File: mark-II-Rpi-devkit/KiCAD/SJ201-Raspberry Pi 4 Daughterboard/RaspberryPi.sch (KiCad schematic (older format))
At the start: 66 parts, among them J6 Raspberry_Pi_4, J7 USB_B_Micro, P1 LED, P2 LED, P3 LED, P4 LED, SW1 MuteMic, U6 FE1.1s, Y2 12MHz

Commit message: SJ201 - Removed CM108b soundcard, added in I2S to Line out, ATTin402. Moved holes in layout. SJ202 - extened length to plug into USB2.0 port
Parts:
- removed TP0, TP1, TP10, TP11, TP12, TP13, TP14, TP15, TP16, TP17, TP19, TP20, TP21, TP26, TP27, TP4, TP5, TP6, TP7, TP8, TP9: TestPoint, TestPoint:TestPoint_Pad_D1.0mm, symbol Connector:TestPoint
- added J13: USB-PinHeader, Connector_PinSocket_2.54mm:PinSocket_1x04_P2.54mm_Horizontal, symbol Connector_Generic:Conn_01x04
- added Prog1: Prog, TestPoint:TestPoint_Pad_D2.0mm, symbol Connector:TestPoint
- added U14: ATtiny402-SS, Package_SO:SOIC-8_3.9x4.9mm_P1.27mm, symbol MCU_Microchip_ATtiny:ATtiny402-SS
- ACT1, P1, P2, P4: MPN 19-217-R6C-AL1M2VY-3T -> 19-217/GHC-YR1S2/3T; SKU 304090042 -> (none)
- D10, D11, D12, D13, D2, D3, D4, D5, D6, D7, D8, D9: LCSC C114583 -> C527089
- DM3, DP3, TP18, TP2, TP3, USB_Power1: MPN (none) -> DNP
- P3: SKU 304090042 -> (none)
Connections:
- net labels added: ATTinyProg, D+, D-, SCL, SDA, USB_MICRO_D+, USB_MICRO_D-
- net labels removed: USB_SOUNDCARD_D+, USB_SOUNDCARD_D-
- wire segments 138 -> 142
- no-connect marks 8 -> 27
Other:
- moved on the sheet: S1, S2, S3, SW1, TP2, TP3

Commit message: SJ-201 v3, sent to PCB Fab. Removed USB Hub, add in I2S to Line Out
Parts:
- removed USB_Power1: USB Jumper, Jumper:SolderJumper-2_P1.3mm_Open_TrianglePad1.0x1.5mm, symbol Connector_Generic:Conn_01x02
- added R12, R13, R14, R15, R16, R19, R9: 0R, Resistor_SMD:R_0603_1608Metric, symbol Device:R_Small
- added R57: 0R - DNP, Resistor_SMD:R_0603_1608Metric, symbol Device:R_Small
- J13: Tempo (none) -> PPTC041LGBN-RC
- J7: Link (none) -> https://www.newark.com/gct-global-connector-technology/usb3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; MPN U254-051T-4BH83-F1B -> USB3076-30-A; Vendor (none) -> Newark
- R30: Tempo (none) -> ERJ-2GEJ104X
- R31: Tempo (none) -> RC0603FR-072K7L
- S1: value Action -> Button
- S2: value VolUp -> Button
- S3: value VolDown -> Button
- Y2: Tempo (none) -> CX3225GB12000D0HEQZ1
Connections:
- net labels added: USB_CORAL_D+, USB_CORAL_D-
- net labels removed: USB_MICRO_D+, USB_MICRO_D-
- wire segments 142 -> 156
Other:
- moved on the sheet: Prog1

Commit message: Rev4 Update - Add in Coral TPU, TAS5806, remove I2S * MAX9744. Change Attiny to Attin1614
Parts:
- removed ACT1, P1, P2, P3, P4: LED, LED_SMD:LED_0603_1608Metric, symbol Device:LED
- removed J7: USB_B_Micro, user:USB_Micro-B_GCT_USB3076-30-A, symbol Connector:USB_B_Micro
- removed Prog1: Prog, TestPoint:TestPoint_Pad_D2.0mm, symbol Connector:TestPoint
- removed R16: 0R, Resistor_SMD:R_0603_1608Metric, symbol Device:R_Small
- removed R29, R33, R38: 330R, Resistor_SMD:R_0402_1005Metric, symbol Device:R_Small
- removed TP3: TestPoint, TestPoint:TestPoint_Pad_D1.0mm, symbol Connector:TestPoint
- removed U14: ATtiny402-SS, Package_SO:SOIC-8_3.9x4.9mm_P1.27mm, symbol MCU_Microchip_ATtiny:ATtiny402-SS
- added J12: FanConnector, Connector:FanPinHeader_1x04_P2.54mm_Vertical, symbol Connector_Generic:Conn_01x04
- added J2: USB_C, Connector_USB:USB_C_Receptacle_XKB_U262-16XN-4BVC11, symbol Connector:USB_C_Receptacle_USB2.0
- added R11, R17, R21: 10k, Resistor_SMD:R_0402_1005Metric, symbol Device:R_Small
- added R18, R20: 5.1k, Resistor_SMD:R_0402_1005Metric, symbol Device:R_Small
- added U13: ATtiny1614-SS, Package_SO:SOIC-14_3.9x8.7mm_P1.27mm, symbol MCU_Microchip_ATtiny:ATtiny1614-SS
- TP2: value TestPoint -> ATTinyProg; footprint TestPoint:TestPoint_Pad_D1.0mm -> TestPoint:TestPoint_Pad_D2.0mm; MPN DNP -> (none)
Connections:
- net labels added: Boot_Sel, Enable1V, FanPWM, FanTemp, I2S_BCLK_PI, I2S_DIN_PI, I2S_DOUT_PI, I2S_LRCK_PI, I2S_MCLK_PI, Neopixel, SPI_CLK, SPI_CSn, SPI_MISO, SPI_MOSI, TPU_INTR, TPU_PGOOD, TPU_PMIC_EN, TPU_RST_L, UART_RXD_PI, UART_TXD_PI, XMOS_SendReset
- net labels removed: ATTinyProg, GPIO18, GPIO4
- wire segments 156 -> 157
- no-connect marks 27 -> 18
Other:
- note added: "Coral TPU"
- note added: "GPIO #18 - I2S Clock\nGPIO #19 - I2S LR Clock (also sometimes called WS Clock)\nGPIO #21 - I2S Data Into the amplifier (out from Pi)\n\nGPIO #16 - Mute pin, you can use this to mute the output complete, \nsometimes helpful if you want to keep audio running and then turn \nit on/off with a switch or button.\nGPIO #20 - I2S Data Out from a microphone (into the Pi)"
- note added: "NeoPixels must be connected to \nGPIO10, GPIO12, GPIO18 or GPIO21 to work! \nGPIO18 is the standard pin."
- note added: "TODO: Check Fan\n Connector Wiring"
- note added: "ToDo: Add PWM Fan Controller"
- note added: "https://github.com/SpenceKonde/megaTinyCore/blob/master/megaavr/extras/ATtiny_x14.md"
- moved on the sheet: C29, C30, C31, C32, C33, C34, DM3, DP3, J13, J6, R12, R13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

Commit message: Rev4 Update - fix some wiring, export for printing Rev 4
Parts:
- removed J12: FanConnector, Connector:FanPinHeader_1x04_P2.54mm_Vertical, symbol Connector_Generic:Conn_01x04
- removed J2: USB_C, Connector_USB:USB_C_Receptacle_XKB_U262-16XN-4BVC11, symbol Connector:USB_C_Receptacle_USB2.0
- removed R18, R20: 5.1k, Resistor_SMD:R_0402_1005Metric, symbol Device:R_Small
- R9: value 0R -> 4.7k; footprint Resistor_SMD:R_0603_1608Metric -> Resistor_SMD:R_0402_1005Metric; LCSC C21189 -> C25900; MPN 0603WAF0000T5E -> 0402WGF4701TCE; Tempo RC0603JR-070RL -> RC0402JR-074K7L
- U13: LCSC (none) -> C481364
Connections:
- net labels added: ATtinyRESET, FanTach
- net labels removed: FanTemp
- wire segments 157 -> 138
- no-connect marks 18 -> 15
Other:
- note removed: "TODO: Check Fan\n Connector Wiring"
- moved on the sheet: J13, TP2

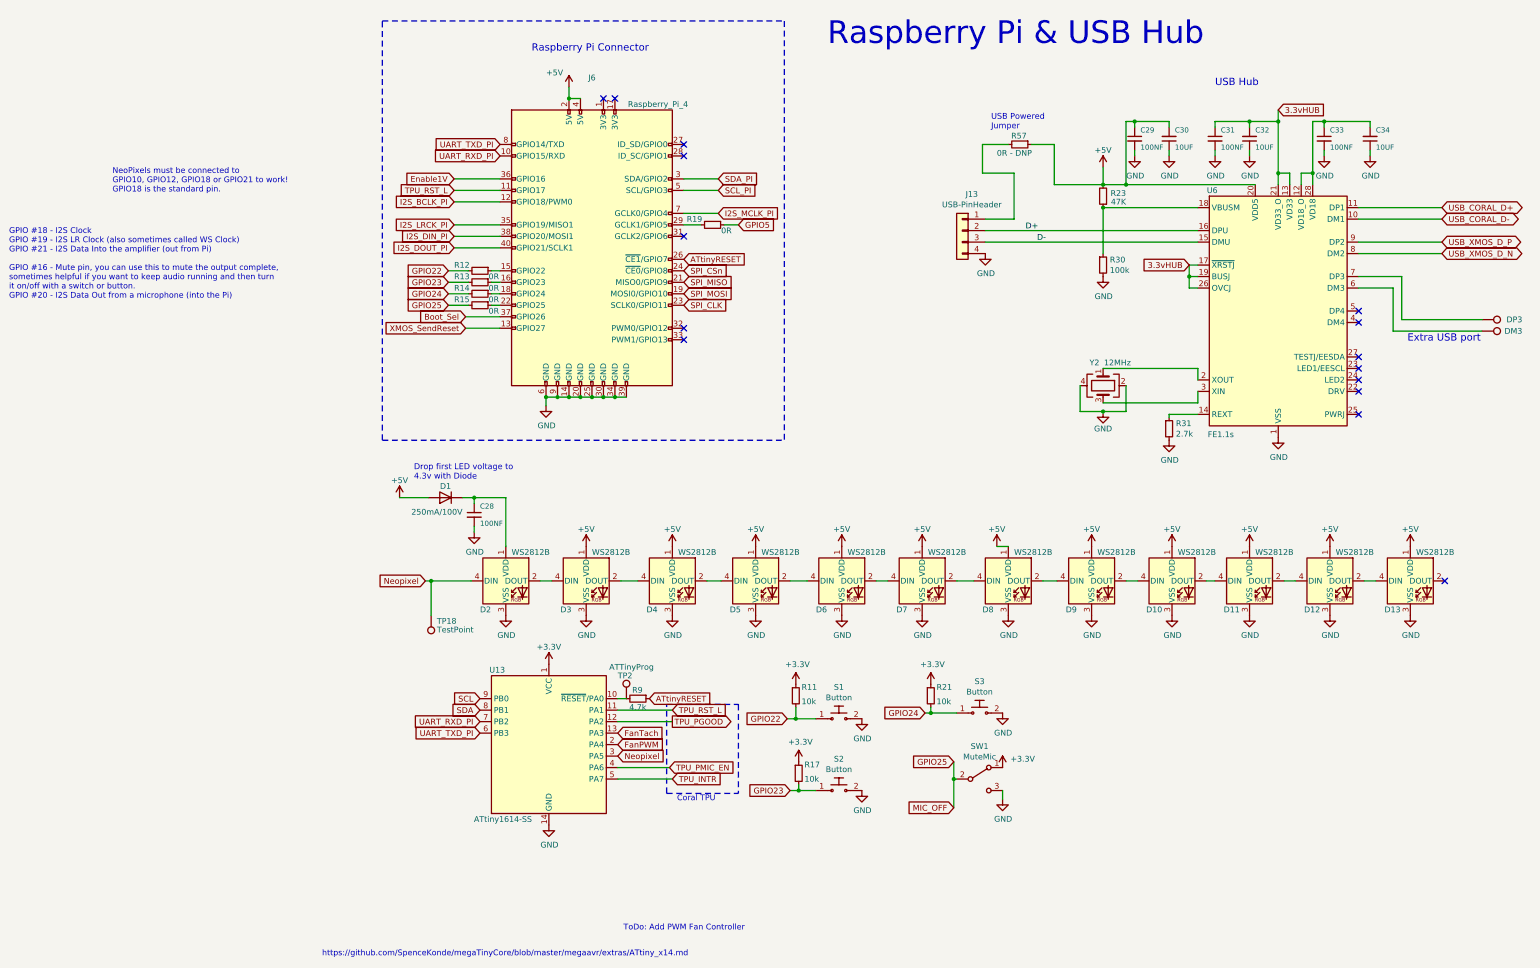
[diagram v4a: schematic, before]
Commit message: SJ-201-R6 for FAB - removed buffer IC
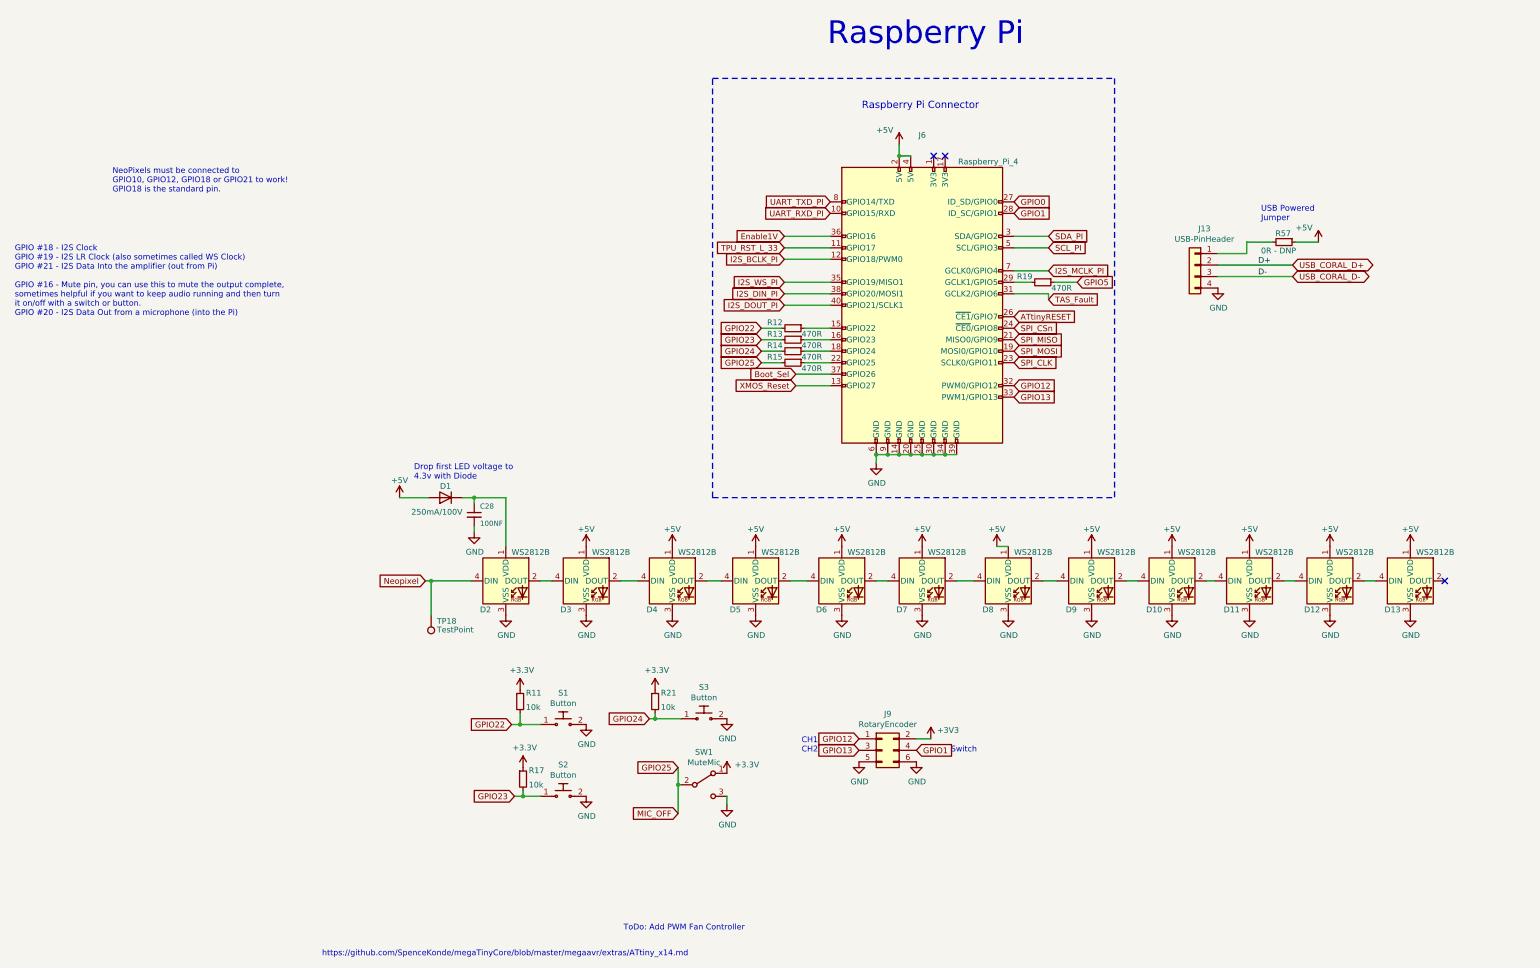
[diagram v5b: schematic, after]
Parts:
- removed C29, C31, C33: 100NF, Capacitor_SMD:C_0402_1005Metric, symbol Device:C_Small
- removed C30, C32, C34: 10UF, Capacitor_SMD:C_0402_1005Metric, symbol Device:C_Small
- removed DM3, DP3: TestPoint, TestPoint:TestPoint_Pad_D1.0mm, symbol Connector:TestPoint
- removed R23: 47K, Resistor_SMD:R_0402_1005Metric, symbol Device:R_Small
- removed R30: 100k, Resistor_SMD:R_0402_1005Metric, symbol Device:R_Small
- removed R31: 2.7k, Resistor_SMD:R_0603_1608Metric, symbol Device:R_Small
- removed R9: 4.7k, Resistor_SMD:R_0402_1005Metric, symbol Device:R_Small
- removed TP2: ATTinyProg, TestPoint:TestPoint_Pad_D2.0mm, symbol Connector:TestPoint
- removed U13: ATtiny1614-SS, Package_SO:SOIC-14_3.9x8.7mm_P1.27mm, symbol MCU_Microchip_ATtiny:ATtiny1614-SS
- removed U6: FE1.1s, Package_SO:SSOP-28_3.9x9.9mm_P0.635mm, symbol Interface_USB:FE1.1s
- removed Y2: 12MHz, Crystal:Crystal_SMD_3225-4Pin_3.2x2.5mm, symbol Device:Crystal_GND24
- added J9: RotaryEncoder, Connector_PinHeader_2.54mm:PinHeader_2x03_P2.54mm_Vertical, symbol Connector_Generic:Conn_02x03_Odd_Even
- R12, R13, R14, R19: value 0R -> 470R; LCSC C21189 -> C23179; MPN 0603WAF0000T5E -> 0603WAF4700T5E; Tempo RC0603JR-070RL -> (none)
- R15: value 0R -> 470R; LCSC C21189 -> (none); Link (none) -> C23179; MPN 0603WAF0000T5E -> 0603WAF4700T5E; Tempo RC0603JR-070RL -> (none)
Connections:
- net D+ is gone; now on net USB_CORAL_D+: J13.2 (Pin_2)
- net D- is gone; now on net USB_CORAL_D-: J13.3 (Pin_3)
- net +3V3: now also J9.2 (Pin_2)
- net GND: now also J9.5 (Pin_5), J9.6 (Pin_6)
- net GPIO0: now reaches J6.27 (ID_SD/GPIO0)
- net GPIO1: now reaches J6.28 (ID_SC/GPIO1)
- net GPIO1: now also J9.4 (Pin_4)
- net TAS_Fault: now reaches J6.31 (GCLK2/GPIO6)
- net GPIO12: now reaches J6.32 (PWM0/GPIO12)
- net GPIO12: now also J9.1 (Pin_1)
- net GPIO13: now reaches J6.33 (PWM1/GPIO13)
- net GPIO13: now also J9.3 (Pin_3)
- net I2S_LRCK_PI renamed I2S_WS_PI
- net TPU_RST_L renamed TPU_RST_L_33
- net XMOS_SendReset renamed XMOS_Reset
- no-connect marks 15 -> 3
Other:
- note added: "CH1\nCH2\n"
- note added: "Raspberry Pi"
- note added: "Switch"
- note removed: "Coral TPU"
- note removed: "Extra USB port\n"
- note removed: "Raspberry Pi & USB Hub"
- note removed: "USB Hub"
- moved on the sheet: J13, J6, R11, R12, R13, R14, R15, R17, R21, R57, S1, S2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

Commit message: Removed unused files, cleaned up directory, remove SJ202
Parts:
- D10, D11, D12, D13, D2, D3, D4, D5, D6, D7, D8, D9: footprint user:LED_WS2812_Mini_3.5x3.5mm_P1.1mm -> Mycroft:LED_WS2812_Mini_3.5x3.5mm_P1.1mm
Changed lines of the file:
@@
 F 0 "D13" H 9225 5325 50  0000 L CNN
 F 1 "WS2812B" H 9500 5825 50  0000 L CNN
-F 2 "user:LED_WS2812_Mini_3.5x3.5mm_P1.1mm" H 9500 5275 50  0001 L TNN
+F 2 "Mycroft:LED_WS2812_Mini_3.5x3.5mm_P1.1mm" H 9500 5275 50  0001 L TNN
 F 3 "http://www.world-semi.com/DownLoadFile/112" H 9550 5200 50  0001 L TNN
 F 4 "WS2812B-MINI(WS2812B-3535)" H 9450 5575 50  0001 C CNN "MPN"
@@
 F 0 "D9" H 6450 5325 50  0000 L CNN
 F 1 "WS2812B" H 6725 5825 50  0000 L CNN
-F 2 "user:LED_WS2812_Mini_3.5x3.5mm_P1.1mm" H 6725 5275 50  0001 L TNN
+F 2 "Mycroft:LED_WS2812_Mini_3.5x3.5mm_P1.1mm" H 6725 5275 50  0001 L TNN
 F 3 "http://www.world-semi.com/DownLoadFile/112" H 6775 5200 50  0001 L TNN
 F 4 "WS2812B-MINI(WS2812B-3535)" H 6675 5575 50  0001 C CNN "MPN"
@@
 F 0 "D2" H 1350 5325 50  0000 L CNN
 F 1 "WS2812B" H 1625 5825 50  0000 L CNN
-F 2 "user:LED_WS2812_Mini_3.5x3.5mm_P1.1mm" H 1625 5275 50  0001 L TNN
+F 2 "Mycroft:LED_WS2812_Mini_3.5x3.5mm_P1.1mm" H 1625 5275 50  0001 L TNN
 F 3 "http://www.world-semi.com/DownLoadFile/112" H 1675 5200 50  0001 L TNN
 F 4 "WS2812B-Mini" H 1575 5575 50  0001 C CNN "MPN"
@@
 F 0 "D12" H 8525 5325 50  0000 L CNN
 F 1 "WS2812B" H 8800 5825 50  0000 L CNN
-F 2 "user:LED_WS2812_Mini_3.5x3.5mm_P1.1mm" H 8800 5275 50  0001 L TNN
+F 2 "Mycroft:LED_WS2812_Mini_3.5x3.5mm_P1.1mm" H 8800 5275 50  0001 L TNN
 F 3 "http://www.world-semi.com/DownLoadFile/112" H 8850 5200 50  0001 L TNN
 F 4 "WS2812B-MINI(WS2812B-3535)" H 8750 5575 50  0001 C CNN "MPN"
@@
 F 0 "D11" H 7825 5325 50  0000 L CNN
 F 1 "WS2812B" H 8100 5825 50  0000 L CNN
-F 2 "user:LED_WS2812_Mini_3.5x3.5mm_P1.1mm" H 8100 5275 50  0001 L TNN
+F 2 "Mycroft:LED_WS2812_Mini_3.5x3.5mm_P1.1mm" H 8100 5275 50  0001 L TNN
 F 3 "http://www.world-semi.com/DownLoadFile/112" H 8150 5200 50  0001 L TNN
 F 4 "WS2812B-MINI(WS2812B-3535)" H 8050 5575 50  0001 C CNN "MPN"
@@
 F 0 "D10" H 7150 5325 50  0000 L CNN
 F 1 "WS2812B" H 7425 5825 50  0000 L CNN
-F 2 "user:LED_WS2812_Mini_3.5x3.5mm_P1.1mm" H 7425 5275 50  0001 L TNN
+F 2 "Mycroft:LED_WS2812_Mini_3.5x3.5mm_P1.1mm" H 7425 5275 50  0001 L TNN
 F 3 "http://www.world-semi.com/DownLoadFile/112" H 7475 5200 50  0001 L TNN
 F 4 "WS2812B-MINI(WS2812B-3535)" H 7375 5575 50  0001 C CNN "MPN"
@@
 F 0 "D3" H 2050 5325 50  0000 L CNN
 F 1 "WS2812B" H 2325 5825 50  0000 L CNN
-F 2 "user:LED_WS2812_Mini_3.5x3.5mm_P1.1mm" H 2325 5275 50  0001 L TNN
+F 2 "Mycroft:LED_WS2812_Mini_3.5x3.5mm_P1.1mm" H 2325 5275 50  0001 L TNN
 F 3 "http://www.world-semi.com/DownLoadFile/112" H 2375 5200 50  0001 L TNN
 F 4 "WS2812B-MINI(WS2812B-3535)" H 2275 5575 50  0001 C CNN "MPN"
@@
 F 0 "D4" H 2800 5325 50  0000 L CNN
 F 1 "WS2812B" H 3075 5825 50  0000 L CNN
-F 2 "user:LED_WS2812_Mini_3.5x3.5mm_P1.1mm" H 3075 5275 50  0001 L TNN
+F 2 "Mycroft:LED_WS2812_Mini_3.5x3.5mm_P1.1mm" H 3075 5275 50  0001 L TNN
 F 3 "http://www.world-semi.com/DownLoadFile/112" H 3125 5200 50  0001 L TNN
 F 4 "WS2812B-MINI(WS2812B-3535)" H 3025 5575 50  0001 C CNN "MPN"
@@
 F 0 "D5" H 3525 5325 50  0000 L CNN
 F 1 "WS2812B" H 3800 5825 50  0000 L CNN
-F 2 "user:LED_WS2812_Mini_3.5x3.5mm_P1.1mm" H 3800 5275 50  0001 L TNN
+F 2 "Mycroft:LED_WS2812_Mini_3.5x3.5mm_P1.1mm" H 3800 5275 50  0001 L TNN
 F 3 "http://www.world-semi.com/DownLoadFile/112" H 3850 5200 50  0001 L TNN
 F 4 "WS2812B-MINI(WS2812B-3535)" H 3750 5575 50  0001 C CNN "MPN"
@@
 F 0 "D6" H 4275 5325 50  0000 L CNN
 F 1 "WS2812B" H 4550 5825 50  0000 L CNN
-F 2 "user:LED_WS2812_Mini_3.5x3.5mm_P1.1mm" H 4550 5275 50  0001 L TNN
+F 2 "Mycroft:LED_WS2812_Mini_3.5x3.5mm_P1.1mm" H 4550 5275 50  0001 L TNN
 F 3 "http://www.world-semi.com/DownLoadFile/112" H 4600 5200 50  0001 L TNN
 F 4 "WS2812B-MINI(WS2812B-3535)" H 4500 5575 50  0001 C CNN "MPN"
@@
 F 0 "D7" H 4975 5325 50  0000 L CNN
 F 1 "WS2812B" H 5250 5825 50  0000 L CNN
-F 2 "user:LED_WS2812_Mini_3.5x3.5mm_P1.1mm" H 5250 5275 50  0001 L TNN
+F 2 "Mycroft:LED_WS2812_Mini_3.5x3.5mm_P1.1mm" H 5250 5275 50  0001 L TNN
 F 3 "http://www.world-semi.com/DownLoadFile/112" H 5300 5200 50  0001 L TNN
 F 4 "WS2812B-MINI(WS2812B-3535)" H 5200 5575 50  0001 C CNN "MPN"
@@
 F 0 "D8" H 5725 5325 50  0000 L CNN
 F 1 "WS2812B" H 6000 5825 50  0000 L CNN
-F 2 "user:LED_WS2812_Mini_3.5x3.5mm_P1.1mm" H 6000 5275 50  0001 L TNN
+F 2 "Mycroft:LED_WS2812_Mini_3.5x3.5mm_P1.1mm" H 6000 5275 50  0001 L TNN
 F 3 "http://www.world-semi.com/DownLoadFile/112" H 6050 5200 50  0001 L TNN
 F 4 "WS2812B-MINI(WS2812B-3535)" H 5950 5575 50  0001 C CNN "MPN"
